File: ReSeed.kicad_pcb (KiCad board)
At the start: 2 copper layers, 60.8 x 99.9 mm, 45 parts, among them CN1 EDGE_CONNECTOR, CN2 AUDIO_OUT, CN3 AUDIO_IN, CN4 DB9_MALE, Q1 2SC1815, SW1 SW_DIGIFIX, U1 MOS_8580, U2 CD4520BE, U3 74LS245, U4 GAL16V8, U5 TL497ACN

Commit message: Stehe ich in Flammen
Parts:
- moved R7 3.81 mm to (142.4, 75.9)
- moved C4 3.54 mm to (125.2, 77.4)
- moved C9 3.17 mm to (138.6, 75.9)
- moved C3 2.54 mm to (134.7, 75.9)
- moved C2 1.73 mm to (130.9, 80.9), turned to 90 degrees
- moved C7 1.40 mm to (146.2, 79.1)
- moved C8 1.40 mm to (150.0, 79.1)
- moved R4 1.40 mm to (146.2, 66.7)
- moved R5 1.40 mm to (150.0, 66.7)
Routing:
- net Net-(C3-Pad1): track 23.7 -> 16.8 mm
- net Net-(C2-Pad1): track 38.1 -> 44.8 mm
- net Net-(C4-Pad2): track 18.3 -> 14.0 mm
- net Net-(C9-Pad1): track 40.4 -> 37.4 mm
- net +5V: track 307.5 -> 304.6 mm
- net /poty: track 16.4 -> 15.0 mm
- net /potx: track 22.6 -> 21.2 mm
- net +9V: track 105.0 -> 106.3 mm
- net Net-(CN2-PadR): track 45.5 -> 46.4 mm
- net Net-(C8-Pad1): track 37.3 -> 36.7 mm

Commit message: Und bin ich In Wasser verbrandt
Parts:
- V1: moved to B.Cu
- moved V1 7.28 mm to (174.1, 133.6), turned to 180 degrees
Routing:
- net Net-(C3-Pad1): track 16.8 -> 26.9 mm
- net +5V: track 304.6 -> 309.5 mm
- net +9V: track 106.3 -> 105.7 mm

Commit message: Feuer und Wasser
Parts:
- added C10: 100n, Capacitor_THT:C_Disc_D7.0mm_W2.5mm_P5.00mm, F.Cu at (130.9, 106.3)
- moved C19 9.22 mm to (153.8, 79.1), turned to 270 degrees
- moved R8 8.75 mm to (153.8, 76.5), turned to 90 degrees
- moved C18 7.52 mm to (161.4, 70.5), turned to 0 degrees
- moved C11 5.00 mm to (136.0, 106.3), turned to 270 degrees
- moved L1 3.37 mm to (174.1, 72.2), turned to 90 degrees
- moved RN1 2.54 mm to (177.9, 63.2)
- moved C17 1.27 mm to (157.6, 79.1)
- moved U5 1.27 mm to (161.4, 84.1)
- moved R1 0.38 mm to (146.2, 66.3)
- moved R2 0.38 mm to (150.0, 66.3)
- moved R7 0.38 mm to (129.2, 66.3)
- renumbered C10 to C17, C17 to C18, C18 to C19, C6 to C2, C7 to C3, C8 to C4, C2 to C5, C3 to C6, C5 to C7, C4 to C8, R4 to R1, R11 to R10, R5 to R2, R2 to R3, R1 to R4, R3 to R5, R7 to R6, R8 to R7, R9 to R8, R10 to R9
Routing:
- net Net-(L1-Pad2): track 16.1 -> 32.8 mm
- net /r_~w: track 68.8 -> 60.4 mm, vias 0 -> 1
- net +9V: track 105.7 -> 112.9 mm
- net +5V: track 309.5 -> 305.5 mm
- net Net-(L1-Pad1): track 18.9 -> 15.1 mm
- net Net-(C15-Pad1): track 6.14 -> 4.23 mm
- net Net-(CN4-Pad1): track 51.8 -> 53.5 mm
- net Net-(CN4-Pad2): track 53.9 -> 55.3 mm
- net Net-(RN1-Pad8): track 51.9 -> 51.0 mm
- net Net-(RN1-Pad9): track 52.7 -> 51.9 mm
- net Net-(RN1-Pad7): track 51.1 -> 50.2 mm
- net Net-(CN4-Pad4): track 59.7 -> 60.5 mm
- net Net-(CN4-Pad3): track 56.5 -> 57.0 mm
- net /half_mux: track 79.3 -> 79.8 mm
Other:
- board text added: "* THE VALUES OF SOME COMPONENTS DEPEND UPON THE SID MODEL: - C1/C2: USE 470p FOR 6581, 22n FOR 8580 - R9: 7.87k 1% FOR 8580 - SW1, RV2, R6: DO NOT MOUNT FOR 6581"
- board text added: "C1*"
- board text added: "C2*"
- board text added: "CC-BY-NC-SA SukkoPera/Kinmami 2022 Based on work by Solder/Sinergy github.com/SukkoPera/ReSeed"
- board text added: "MOS 6581/8580*"
- board text added: "R6*"
- board text added: "R9*"
- board text added: "RV2*"
- board text added: "SW1*"
- board text removed: "SukkoPera/Kinmami 2022 Based on work by Solder/Sinergy github.com/SukkoPera/ReSeed"

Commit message: Ready?
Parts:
- added JP1: JMP_GND_LIFT, Jumper:SolderJumper-2_P1.3mm_Bridged_RoundedPad1.0x1.5mm, B.Cu at (143.9, 61.2)
- moved V1 42.5 mm to (163.3, 92.6)
- moved C15 14.1 mm to (157.6, 79.1)
- moved C16 12.7 mm to (174.1, 90.0)
- moved R10 10.2 mm to (162.7, 97.7)
- moved R9 10.2 mm to (166.5, 97.7)
- moved C19 4.62 mm to (157.6, 76.5), turned to 90 degrees
- moved C17 3.81 mm to (153.8, 79.1)
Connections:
- CN3 pad RN: GND -> Net-(CN3-PadRN)
- CN3 pad TN: GND -> Net-(CN3-PadTN)
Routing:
- net Net-(R10-Pad2): track 33.2 -> 17.7 mm
- net Net-(C15-Pad1): track 4.23 -> 12.7 mm
- net Net-(CN4-Pad6): track 70.8 -> 64.5 mm
- net Net-(CN4-Pad4): track 60.5 -> 55.0 mm
- net Net-(CN3-PadTN): track 0.00 -> 3.95 mm
- net Net-(CN4-Pad3): track 57.0 -> 54.0 mm
- net +5V: track 305.5 -> 302.5 mm
- net Net-(CN4-Pad1): track 53.5 -> 56.4 mm
- net GND: track 23.0 -> 24.5 mm, vias 4 -> 6
- net +9V: track 112.9 -> 111.8 mm
- net Net-(CN4-Pad2): track 55.3 -> 54.4 mm
- net /ext_audio: track 141.7 -> 141.0 mm
- net /mux: track 96.1 -> 95.5 mm
- net /phi2: track 111.2 -> 111.8 mm
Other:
- board text added: "* SOME VALUES DEPEND UPON THE SID MODEL: MOS 8580: C1/C2 = 22n, R9 = 7.87k 1%, SW1/RV2/R6 = MOUNT NORMALLY MOS 6581: C1/C2 = 470p, R9 = 11k 1%, SW1/RV2/R6 = DON'T MOUNT"
- board text added: "CC-BY-NC-SA SukkoPera/Kinmami 2022 Based on work by Solder/Synergy github.com/SukkoPera/ReSeed"
- board text removed: "* THE VALUES OF SOME COMPONENTS DEPEND UPON THE SID MODEL: - C1/C2: USE 470p FOR 6581, 22n FOR 8580 - R9: 7.87k 1% FOR 8580 - SW1, RV2, R6: DO NOT MOUNT FOR 6581"
- board text removed: "CC-BY-NC-SA SukkoPera/Kinmami 2022 Based on work by Solder/Sinergy github.com/SukkoPera/ReSeed"

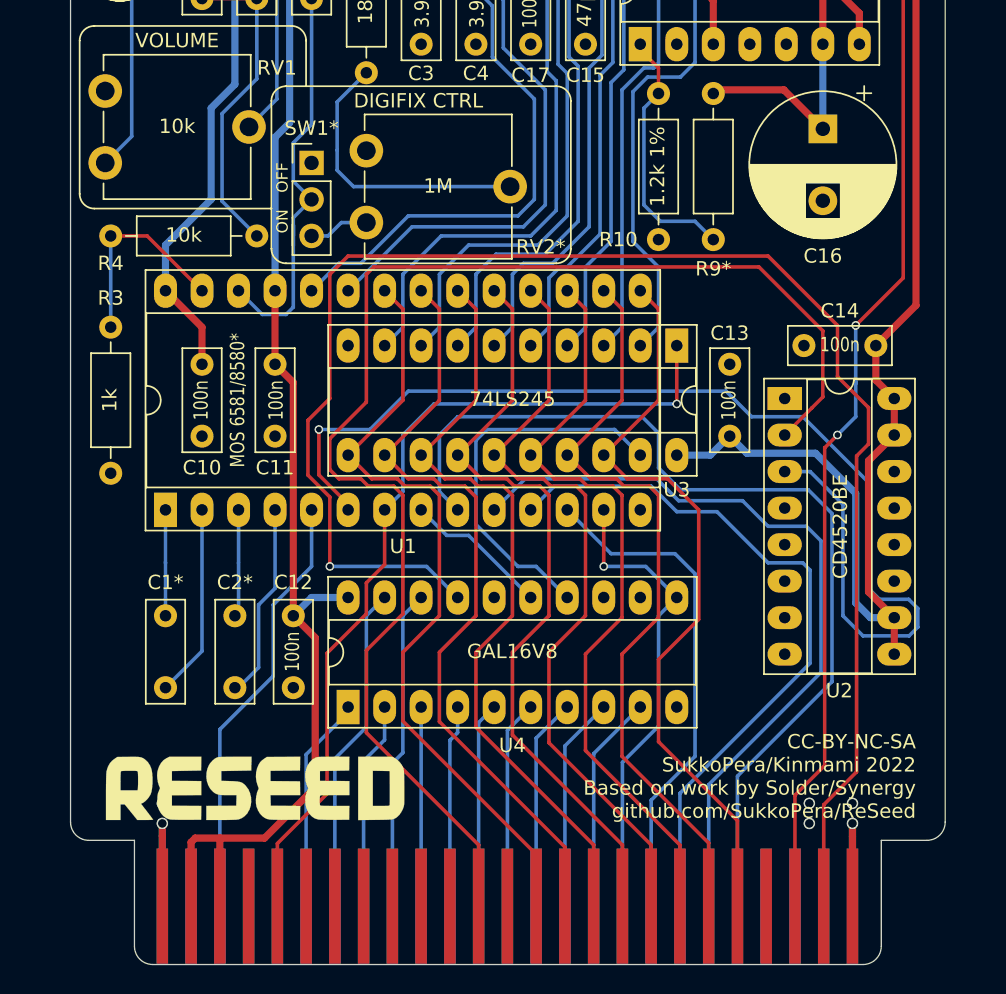
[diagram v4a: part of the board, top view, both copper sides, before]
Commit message: Add note about R3
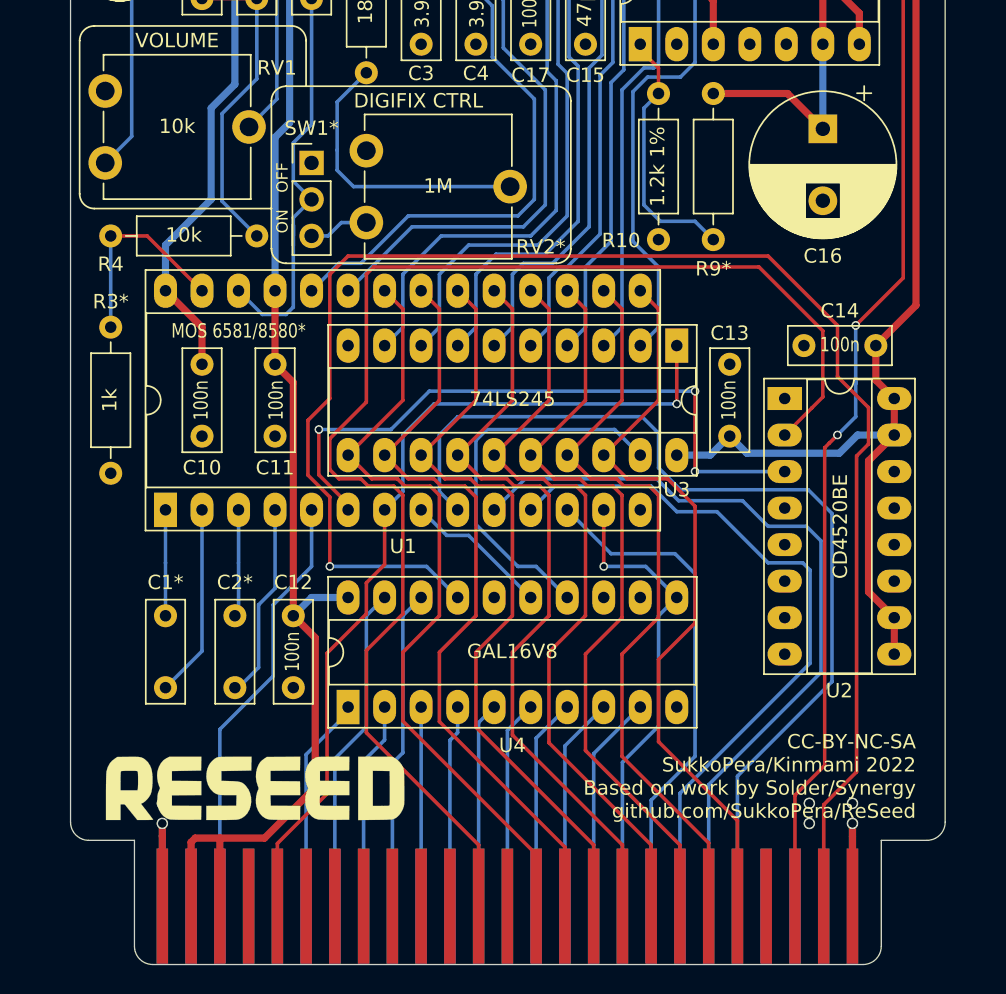
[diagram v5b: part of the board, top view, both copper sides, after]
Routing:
- net /half_mux: track 79.8 -> 45.5 mm, vias 1 -> 3
- net +5V: track 302.5 -> 293.8 mm
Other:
- board text added: "* SOME VALUES DEPEND UPON THE SID MODEL: MOS 8580: C1/C2 = 22n, R9 = 7.87k 1%, SW1/RV2/R3/R6 = MOUNT NORMALLY MOS 6581: C1/C2 = 470p, R9 = 11k 1%, SW1/RV2/R3/R6 = DO NOT MOUNT"
- board text added: "R3*"
- board text removed: "* SOME VALUES DEPEND UPON THE SID MODEL: MOS 8580: C1/C2 = 22n, R9 = 7.87k 1%, SW1/RV2/R6 = MOUNT NORMALLY MOS 6581: C1/C2 = 470p, R9 = 11k 1%, SW1/RV2/R6 = DON'T MOUNT"

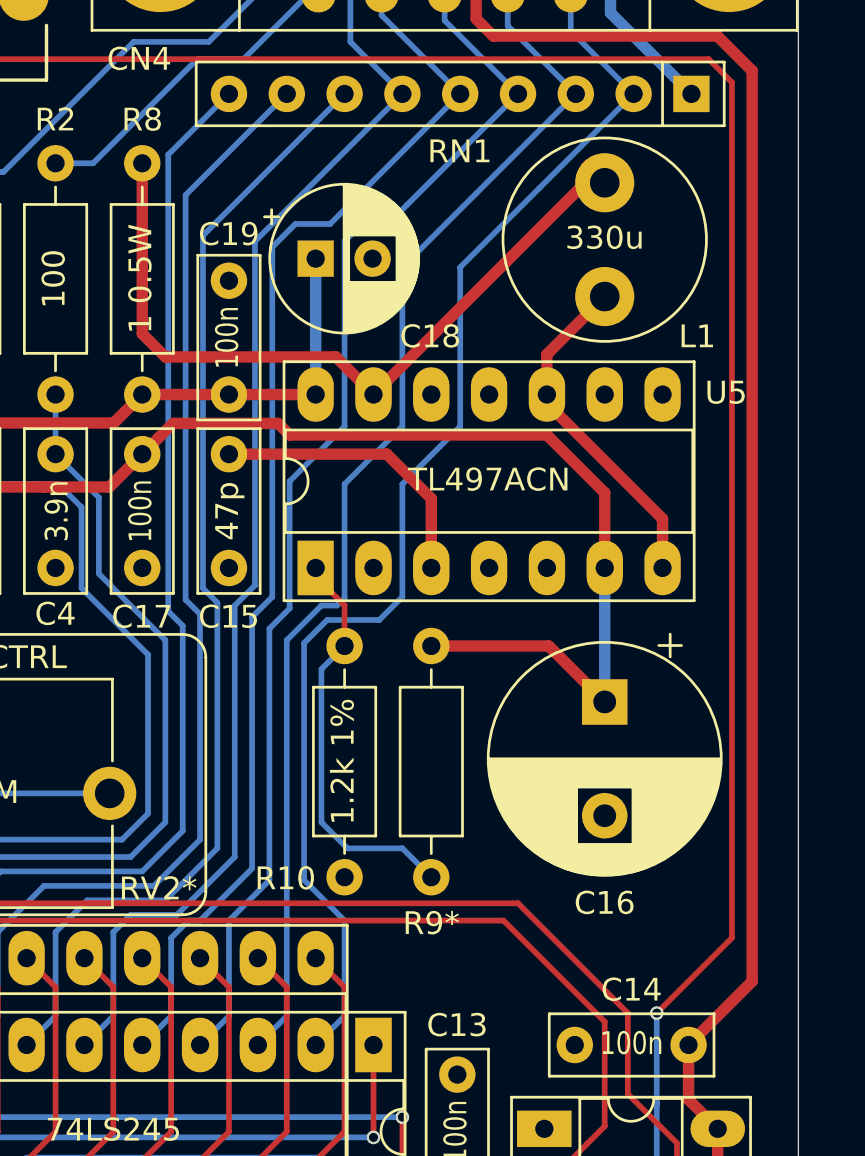
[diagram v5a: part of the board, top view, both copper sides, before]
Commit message: Improve decoupling on U5
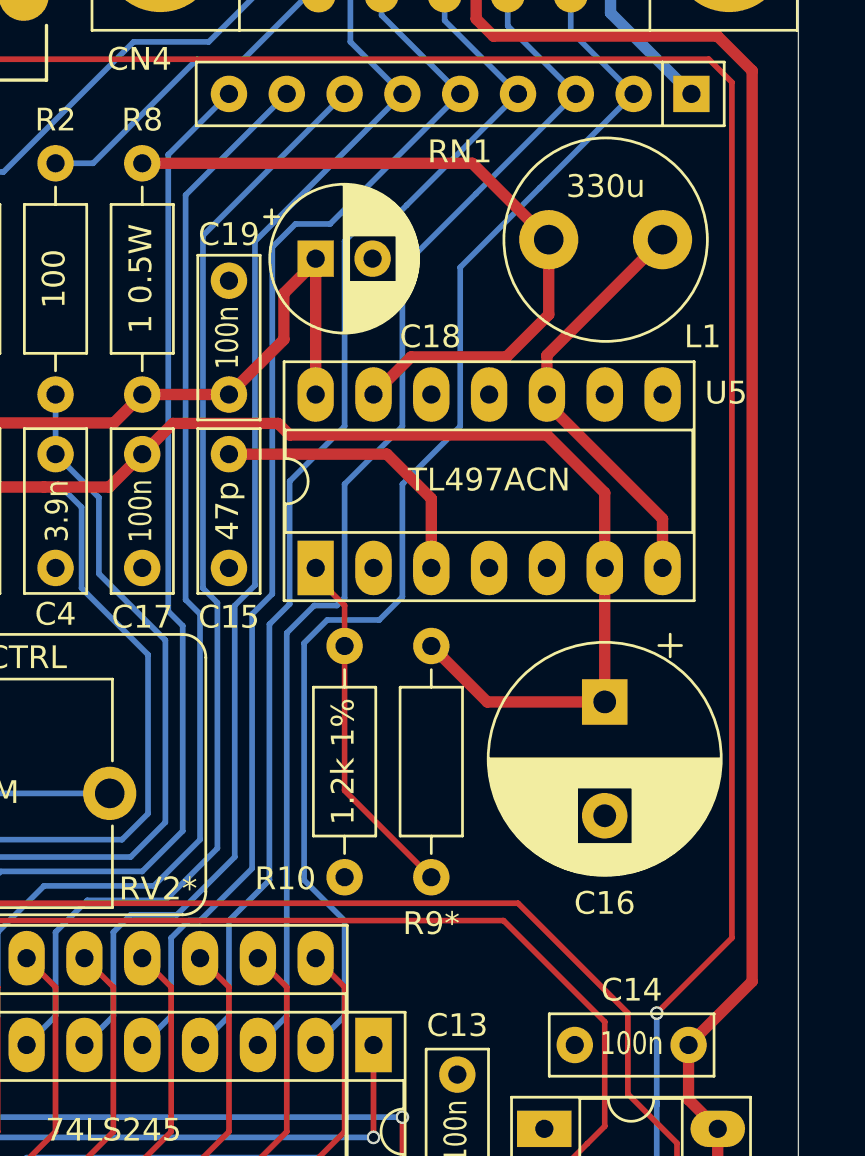
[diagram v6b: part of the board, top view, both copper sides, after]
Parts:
- moved L1 3.56 mm to (176.7, 69.7), turned to 180 degrees
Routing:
- net +5V: track 293.8 -> 297.5 mm
- net Net-(L1-Pad1): track 15.1 -> 18.6 mm
- net Net-(R10-Pad2): track 17.7 -> 15.4 mm
- net Net-(L1-Pad2): track 32.8 -> 31.7 mm
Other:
- board text added: "* SOME VALUES DEPEND UPON THE SID MODEL: - MOS 8580: C1/C2 = 22n, R9 = 7.87k 1%, R3 = DO NOT MOUNT, SW1/RV2/R6 = MOUNT NORMALLY - MOS 6581: C1/C2 = 470p, R9 = 11k 1%, R3 = MOUNT NORMALLY, SW1/RV2/R6 = DO NOT MOUNT"
- board text removed: "* SOME VALUES DEPEND UPON THE SID MODEL: MOS 8580: C1/C2 = 22n, R9 = 7.87k 1%, SW1/RV2/R3/R6 = MOUNT NORMALLY MOS 6581: C1/C2 = 470p, R9 = 11k 1%, SW1/RV2/R3/R6 = DO NOT MOUNT"

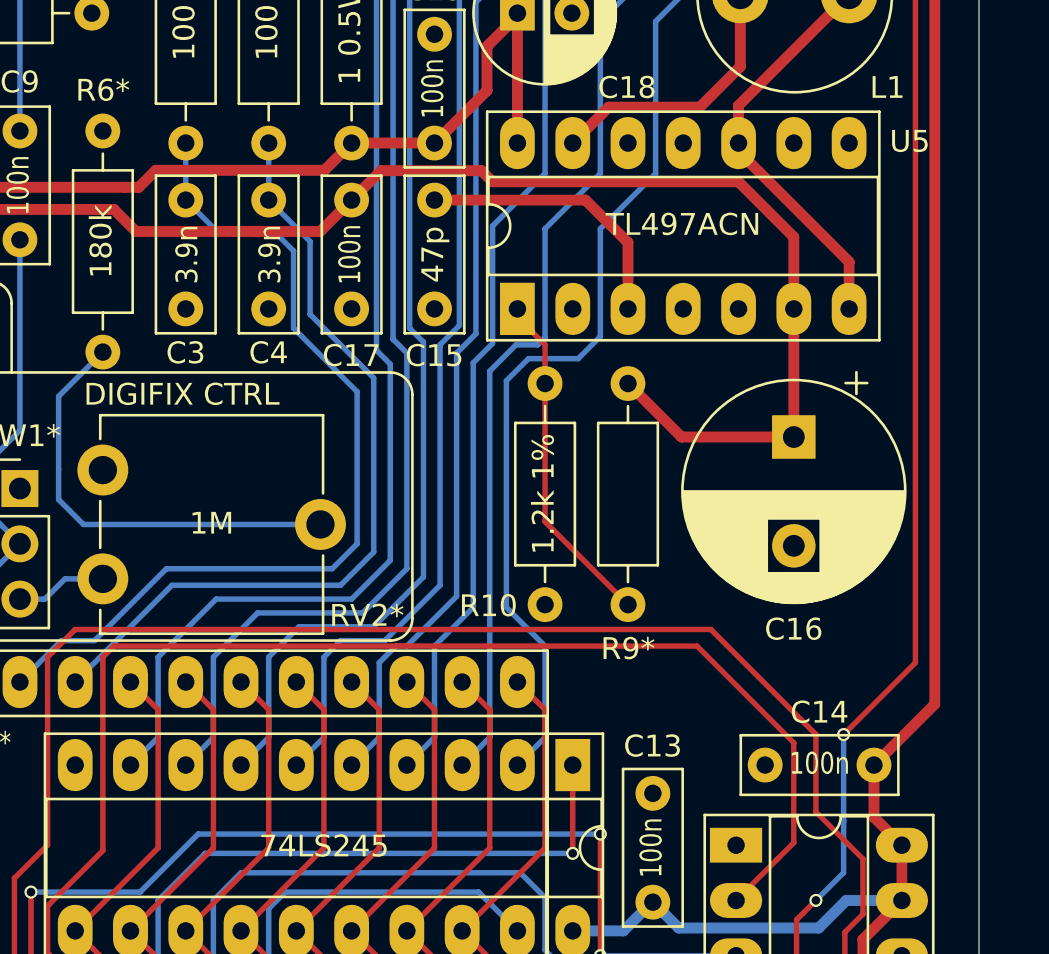
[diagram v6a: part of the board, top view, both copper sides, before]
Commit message: Reroute some tracks around DC/DC converter
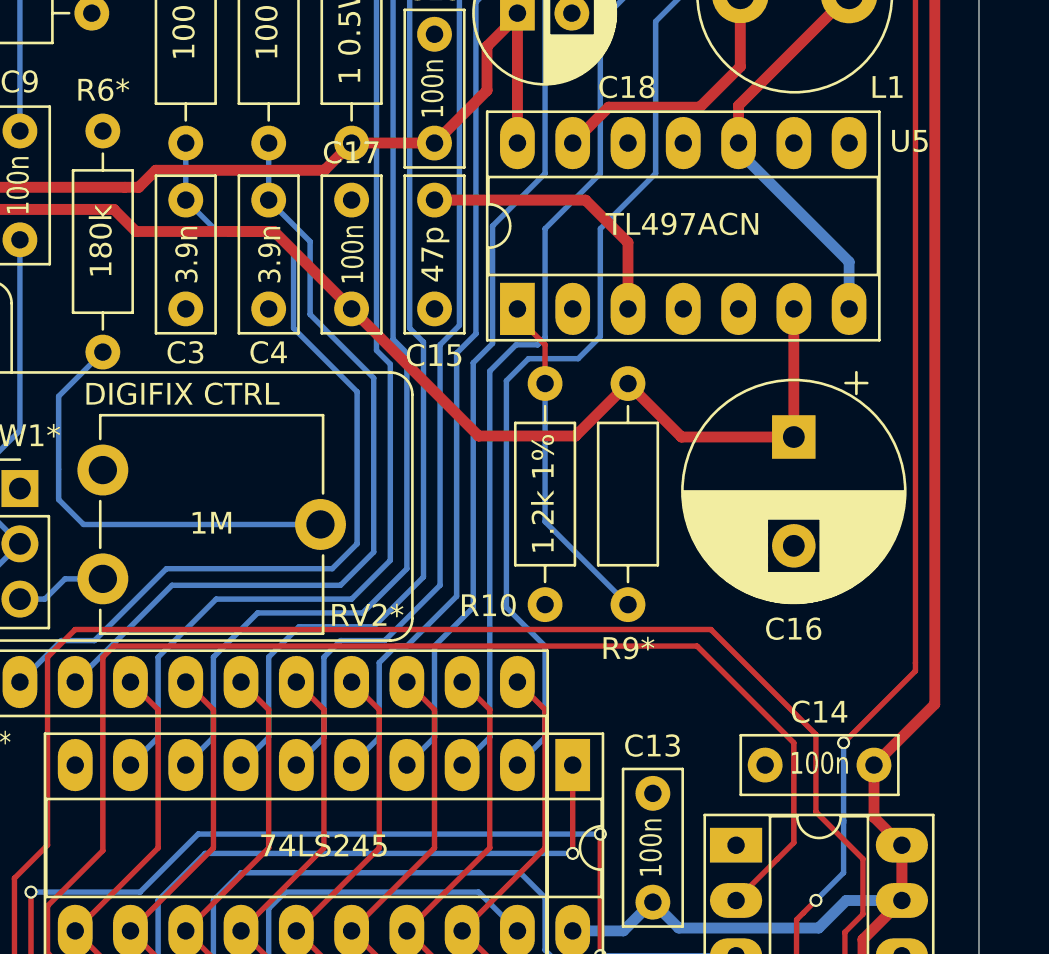
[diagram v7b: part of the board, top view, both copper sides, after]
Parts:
- moved C17 5.00 mm to (153.8, 84.1), turned to 90 degrees
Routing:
- net +9V: track 111.7 -> 104.5 mm
